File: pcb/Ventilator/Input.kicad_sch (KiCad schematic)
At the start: 49 parts, among them J2 Screw_Terminal_01x08, U3 4N25, U4 4N25, U5 4N25, U6 4N25

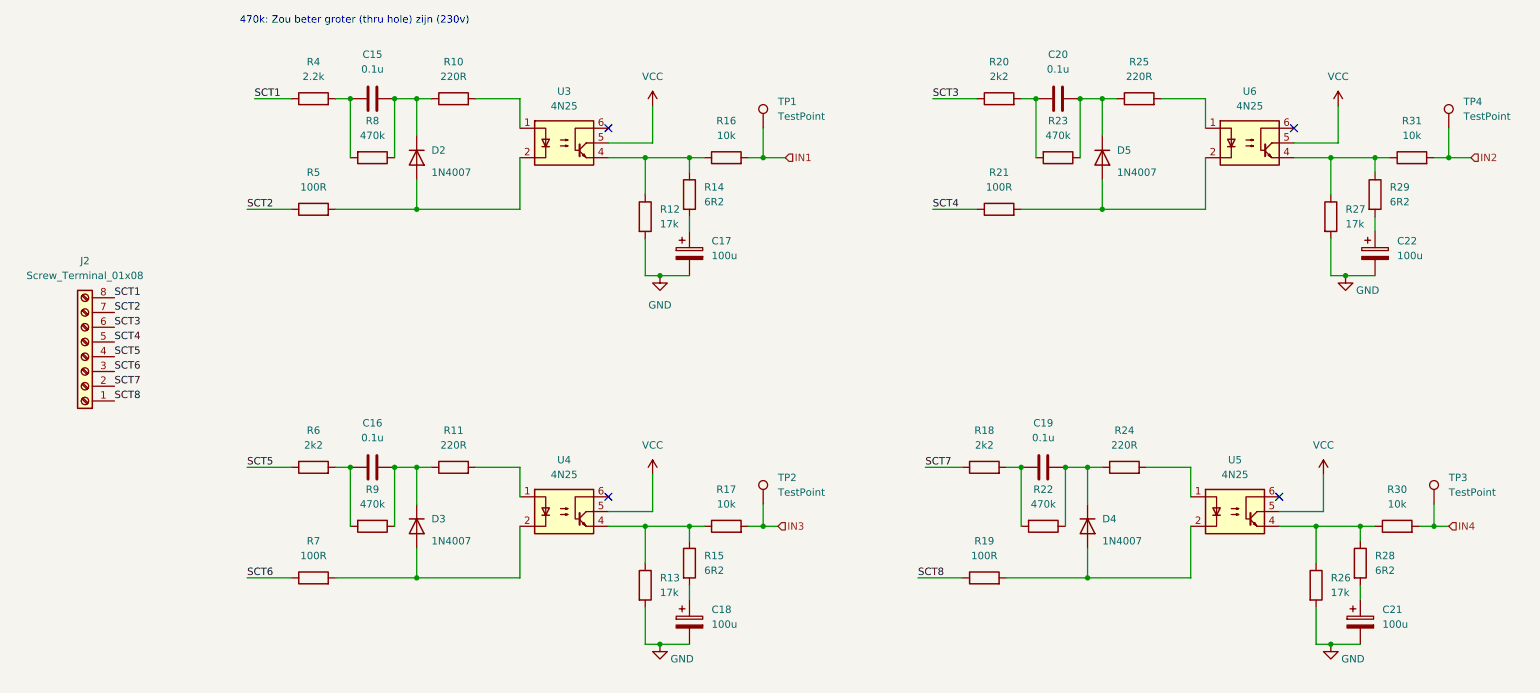
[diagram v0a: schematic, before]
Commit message: - all parts connected, placed partially
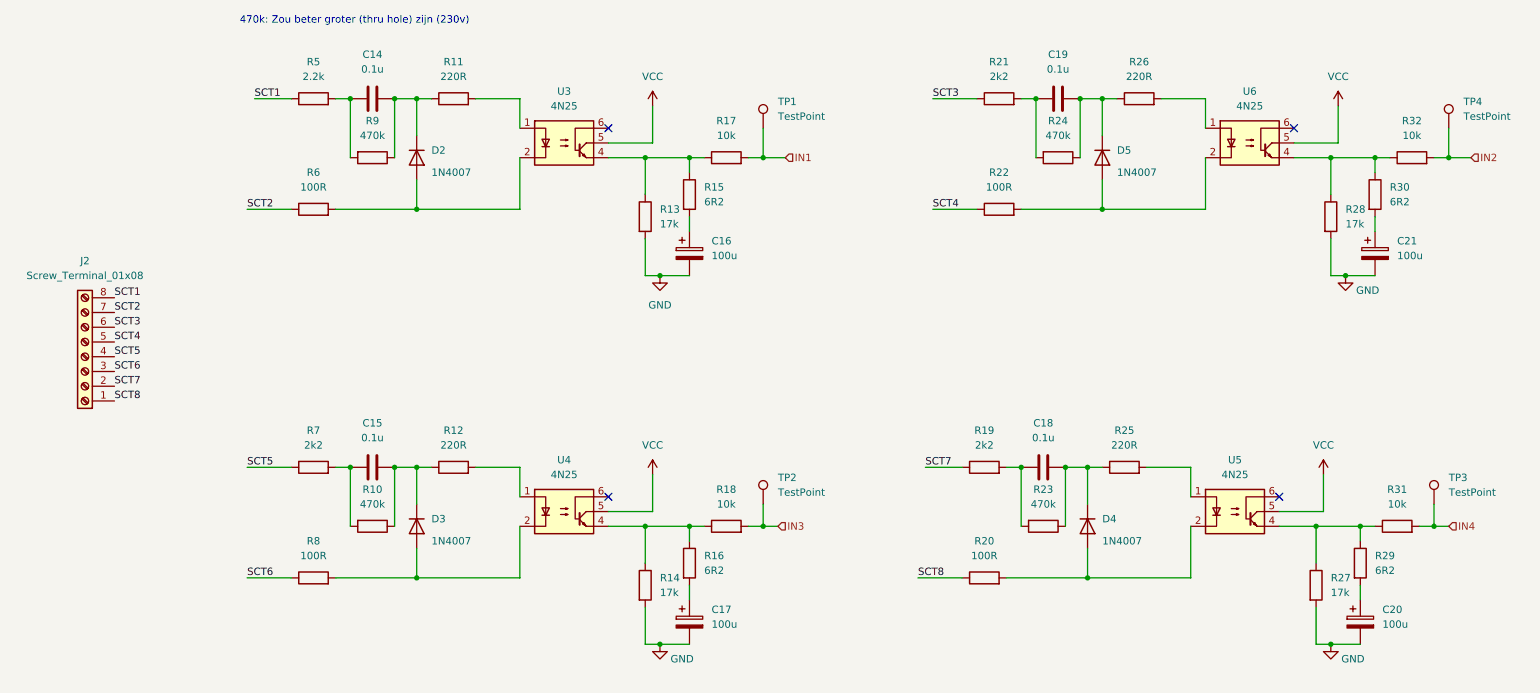
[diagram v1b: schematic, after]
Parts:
- R10: renamed from R9; footprint Resistor_SMD:R_0805_2012Metric_Pad1.20x1.40mm_HandSolder -> Resistor_SMD:R_2512_6332Metric
- R19: renamed from R18; footprint Resistor_THT:R_Axial_DIN0414_L11.9mm_D4.5mm_P15.24mm_Horizontal -> Resistor_SMD:R_2512_6332Metric
- R21: renamed from R20; footprint Resistor_THT:R_Axial_DIN0414_L11.9mm_D4.5mm_P15.24mm_Horizontal -> Resistor_SMD:R_2512_6332Metric
- R23: renamed from R22; footprint Resistor_SMD:R_0805_2012Metric_Pad1.20x1.40mm_HandSolder -> Resistor_SMD:R_2512_6332Metric
- R24: renamed from R23; footprint Resistor_SMD:R_0805_2012Metric_Pad1.20x1.40mm_HandSolder -> Resistor_SMD:R_2512_6332Metric
- R5: renamed from R4; footprint Resistor_THT:R_Axial_DIN0414_L11.9mm_D4.5mm_P15.24mm_Horizontal -> Resistor_SMD:R_2512_6332Metric
- R7: renamed from R6; footprint Resistor_THT:R_Axial_DIN0414_L11.9mm_D4.5mm_P15.24mm_Horizontal -> Resistor_SMD:R_2512_6332Metric
- R9: renamed from R8; footprint Resistor_SMD:R_0805_2012Metric_Pad1.20x1.40mm_HandSolder -> Resistor_SMD:R_2512_6332Metric
- renumbered C15 to C14, C16 to C15, C17 to C16, C18 to C17, C19 to C18, C20 to C19, C21 to C20, C22 to C21, R10 to R11, R11 to R12, R12 to R13, R13 to R14, R14 to R15, R15 to R16, R16 to R17, R17 to R18, R19 to R20, R21 to R22, R24 to R25, R25 to R26, R26 to R27, R27 to R28, R28 to R29, R29 to R30, R30 to R31, R31 to R32, R5 to R6, R7 to R8

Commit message: - voor omschakeling naar rp pico
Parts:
- renumbered C14 to C13, C15 to C14, C16 to C15, C17 to C16, C18 to C17, C19 to C18, C20 to C19, C21 to C20, U3 to U4, U4 to U5, U5 to U6, U6 to U7
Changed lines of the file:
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@@
   (symbol (lib_id "Device:C_Polarized") (at 250.19 55.88 0) (unit 1)
     (in_bom yes) (on_board yes) (fields_autoplaced)
-    (property "Reference" "C21" (id 0) (at 254 53.7209 0)
+    (property "Reference" "C20" (id 0) (at 254 53.7209 0)
       (effects (font (size 1.27 1.27)) (justify left))
     )
@@
   (symbol (lib_id "Device:C_Polarized") (at 247.65 119.38 0) (unit 1)
     (in_bom yes) (on_board yes) (fields_autoplaced)
-    (property "Reference" "C20" (id 0) (at 251.46 117.2209 0)
+    (property "Reference" "C19" (id 0) (at 251.46 117.2209 0)
       (effects (font (size 1.27 1.27)) (justify left))
     )
@@
   (symbol (lib_id "Device:C_Polarized") (at 132.08 119.38 0) (unit 1)
     (in_bom yes) (on_board yes) (fields_autoplaced)
-    (property "Reference" "C17" (id 0) (at 135.89 117.2209 0)
+    (property "Reference" "C16" (id 0) (at 135.89 117.2209 0)
       (effects (font (size 1.27 1.27)) (justify left))
     )
@@
   (symbol (lib_id "Device:C_Polarized") (at 132.08 55.88 0) (unit 1)
     (in_bom yes) (on_board yes) (fields_autoplaced)
-    (property "Reference" "C16" (id 0) (at 135.89 53.7209 0)
+    (property "Reference" "C15" (id 0) (at 135.89 53.7209 0)
       (effects (font (size 1.27 1.27)) (justify left))
     )
@@
   (symbol (lib_id "power:VCC") (at 125.73 93.98 0) (unit 1)
     (in_bom yes) (on_board yes) (fields_autoplaced)
-    (property "Reference" "#PWR015" (id 0) (at 125.73 97.79 0)
+    (property "Reference" "#PWR018" (id 0) (at 125.73 97.79 0)
       (effects (font (size 1.27 1.27)) hide)
     )
@@
   (symbol (lib_id "power:VCC") (at 241.3 93.98 0) (unit 1)
     (in_bom yes) (on_board yes) (fields_autoplaced)
-    (property "Reference" "#PWR018" (id 0) (at 241.3 97.79 0)
+    (property "Reference" "#PWR021" (id 0) (at 241.3 97.79 0)
       (effects (font (size 1.27 1.27)) hide)
     )
@@
   (symbol (lib_id "Device:C") (at 195.58 29.21 270) (unit 1)
     (in_bom yes) (on_board yes) (fields_autoplaced)
-    (property "Reference" "C19" (id 0) (at 195.58 21.59 90))
+    (property "Reference" "C18" (id 0) (at 195.58 21.59 90))
     (property "Value" "0.1u" (id 1) (at 195.58 24.13 90))
     (property "Footprint" "Capacitor_THT:C_Rect_L18.0mm_W5.0mm_P15.00mm_FKS3_FKP3" (id 2) (at 191.77 30.1752 0)
@@
   (symbol (lib_id "Isolator:4N25") (at 226.06 100.33 0) (unit 1)
     (in_bom yes) (on_board yes) (fields_autoplaced)
-    (property "Reference" "U5" (id 0) (at 226.06 91.44 0))
+    (property "Reference" "U6" (id 0) (at 226.06 91.44 0))
     (property "Value" "4N25" (id 1) (at 226.06 93.98 0))
     (property "Footprint" "Package_DIP:DIP-6_W7.62mm" (id 2) (at 220.98 105.41 0)
@@
   (symbol (lib_id "Isolator:4N25") (at 110.49 100.33 0) (unit 1)
     (in_bom yes) (on_board yes) (fields_autoplaced)
-    (property "Reference" "U4" (id 0) (at 110.49 91.44 0))
+    (property "Reference" "U5" (id 0) (at 110.49 91.44 0))
     (property "Value" "4N25" (id 1) (at 110.49 93.98 0))
     (property "Footprint" "Package_DIP:DIP-6_W7.62mm" (id 2) (at 105.41 105.41 0)
@@
   (symbol (lib_id "power:GND") (at 127 123.19 0) (unit 1)
     (in_bom yes) (on_board yes)
-    (property "Reference" "#PWR017" (id 0) (at 127 129.54 0)
+    (property "Reference" "#PWR020" (id 0) (at 127 129.54 0)
       (effects (font (size 1.27 1.27)) hide)
     )
@@
   (symbol (lib_id "power:GND") (at 245.11 59.69 0) (unit 1)
     (in_bom yes) (on_board yes)
-    (property "Reference" "#PWR021" (id 0) (at 245.11 66.04 0)
+    (property "Reference" "#PWR024" (id 0) (at 245.11 66.04 0)
       (effects (font (size 1.27 1.27)) hide)
     )
@@
   (symbol (lib_id "Isolator:4N25") (at 110.49 36.83 0) (unit 1)
     (in_bom yes) (on_board yes) (fields_autoplaced)
-    (property "Reference" "U3" (id 0) (at 110.49 27.94 0))
+    (property "Reference" "U4" (id 0) (at 110.49 27.94 0))
     (property "Value" "4N25" (id 1) (at 110.49 30.48 0))
     (property "Footprint" "Package_DIP:DIP-6_W7.62mm" (id 2) (at 105.41 41.91 0)
@@
   (symbol (lib_id "power:VCC") (at 125.73 30.48 0) (unit 1)
     (in_bom yes) (on_board yes) (fields_autoplaced)
-    (property "Reference" "#PWR014" (id 0) (at 125.73 34.29 0)
+    (property "Reference" "#PWR017" (id 0) (at 125.73 34.29 0)
       (effects (font (size 1.27 1.27)) hide)
     )
@@
   (symbol (lib_id "power:GND") (at 127 59.69 0) (unit 1)
     (in_bom yes) (on_board yes)
-    (property "Reference" "#PWR016" (id 0) (at 127 66.04 0)
+    (property "Reference" "#PWR019" (id 0) (at 127 66.04 0)
       (effects (font (size 1.27 1.27)) hide)
     )
@@
   (symbol (lib_id "Device:C") (at 193.04 92.71 270) (unit 1)
     (in_bom yes) (on_board yes) (fields_autoplaced)
-    (property "Reference" "C18" (id 0) (at 193.04 85.09 90))
+    (property "Reference" "C17" (id 0) (at 193.04 85.09 90))
     (property "Value" "0.1u" (id 1) (at 193.04 87.63 90))
     (property "Footprint" "Capacitor_THT:C_Rect_L18.0mm_W5.0mm_P15.00mm_FKS3_FKP3" (id 2) (at 189.23 93.6752 0)
@@
   (symbol (lib_id "power:GND") (at 242.57 123.19 0) (unit 1)
     (in_bom yes) (on_board yes)
-    (property "Reference" "#PWR019" (id 0) (at 242.57 129.54 0)
+    (property "Reference" "#PWR022" (id 0) (at 242.57 129.54 0)
       (effects (font (size 1.27 1.27)) hide)
     )
@@
   (symbol (lib_id "Device:C") (at 77.47 29.21 270) (unit 1)
     (in_bom yes) (on_board yes) (fields_autoplaced)
-    (property "Reference" "C14" (id 0) (at 77.47 21.59 90))
+    (property "Reference" "C13" (id 0) (at 77.47 21.59 90))
     (property "Value" "0.1u" (id 1) (at 77.47 24.13 90))
     (property "Footprint" "Capacitor_THT:C_Rect_L18.0mm_W5.0mm_P15.00mm_FKS3_FKP3" (id 2) (at 73.66 30.1752 0)
@@
   (symbol (lib_id "power:VCC") (at 243.84 30.48 0) (unit 1)
     (in_bom yes) (on_board yes) (fields_autoplaced)
-    (property "Reference" "#PWR020" (id 0) (at 243.84 34.29 0)
+    (property "Reference" "#PWR023" (id 0) (at 243.84 34.29 0)
       (effects (font (size 1.27 1.27)) hide)
     )
@@
   (symbol (lib_id "Device:C") (at 77.47 92.71 270) (unit 1)
     (in_bom yes) (on_board yes)
-    (property "Reference" "C15" (id 0) (at 77.47 85.09 90))
+    (property "Reference" "C14" (id 0) (at 77.47 85.09 90))
     (property "Value" "0.1u" (id 1) (at 77.47 87.63 90))
     (property "Footprint" "Capacitor_THT:C_Rect_L18.0mm_W5.0mm_P15.00mm_FKS3_FKP3" (id 2) (at 73.66 93.6752 0)
@@
   (symbol (lib_id "Isolator:4N25") (at 228.6 36.83 0) (unit 1)
     (in_bom yes) (on_board yes) (fields_autoplaced)
-    (property "Reference" "U6" (id 0) (at 228.6 27.94 0))
+    (property "Reference" "U7" (id 0) (at 228.6 27.94 0))
     (property "Value" "4N25" (id 1) (at 228.6 30.48 0))
     (property "Footprint" "Package_DIP:DIP-6_W7.62mm" (id 2) (at 223.52 41.91 0)

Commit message: - voor autorouter
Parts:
- renumbered C13 to C1, C14 to C2, C15 to C3, C16 to C4, C17 to C5, C18 to C6, C19 to C7, C20 to C8, R11 to R10, R12 to R11, R13 to R12, R14 to R13, R15 to R14, R16 to R15, R17 to R16, R18 to R17, R19 to R18, R20 to R19, R21 to R20, R22 to R21, R23 to R22, R24 to R23, R25 to R24, R26 to R25, R27 to R26, R28 to R27, R29 to R28, R30 to R29, R31 to R30, R32 to R31, R5 to R4, R6 to R5, R7 to R6, R8 to R7, R9 to R8, R10 to R9, U4 to U2, U5 to U3, U6 to U4, U7 to U5
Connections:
- net VCC renamed +3.3V

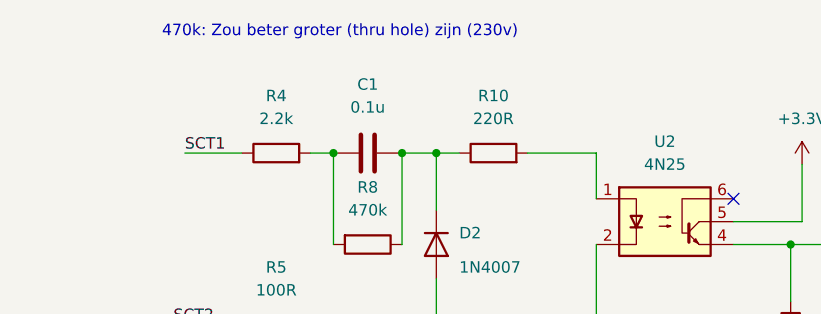
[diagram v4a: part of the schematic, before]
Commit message: -Ventcontrol 1.2 (routed)
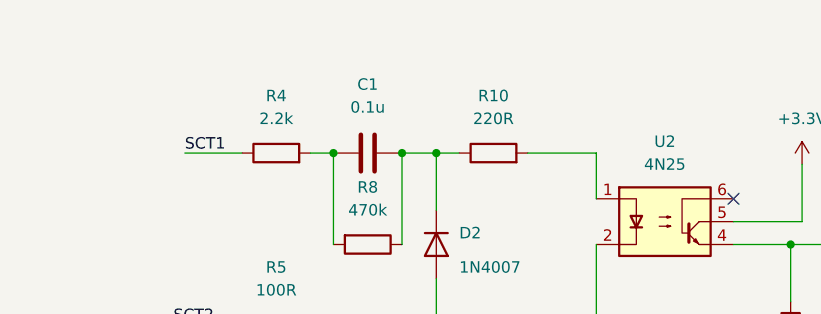
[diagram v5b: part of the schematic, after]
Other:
- note removed: "470k: Zou beter groter (thru hole) zijn (230v)"
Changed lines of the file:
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@@
     (stroke (width 0) (type default) (color 0 0 0 0))
-  )
-  (text "470k: Zou beter groter (thru hole) zijn (230v)" (at 54.61 16.51 0)
-    (effects (font (size 1.27 1.27)) (justify left bottom))
   )
   (label "SCT7" (at 172.72 92.71 0)
